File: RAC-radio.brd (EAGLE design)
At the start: 160 x 100 mm, 24 parts, among them J2 CORTEX_DEBUG_MINIMUM_SMD, J3 U.FL, U1 MAX32660GTP+, U2 RN4871-I_RM130, U3 RFM95W-868S2, Y1 32.768kHz

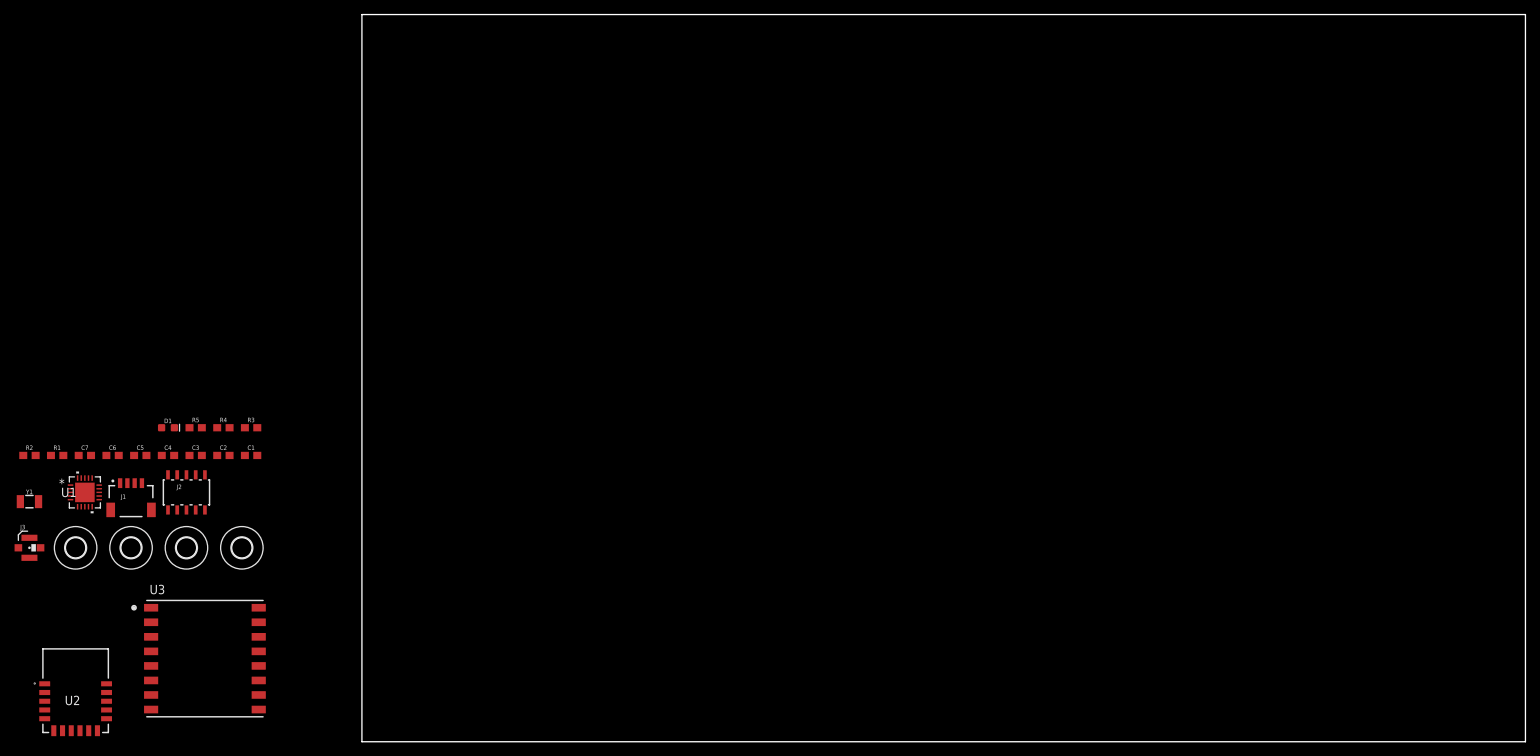
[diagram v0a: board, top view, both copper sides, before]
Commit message: Routed the non-power nets
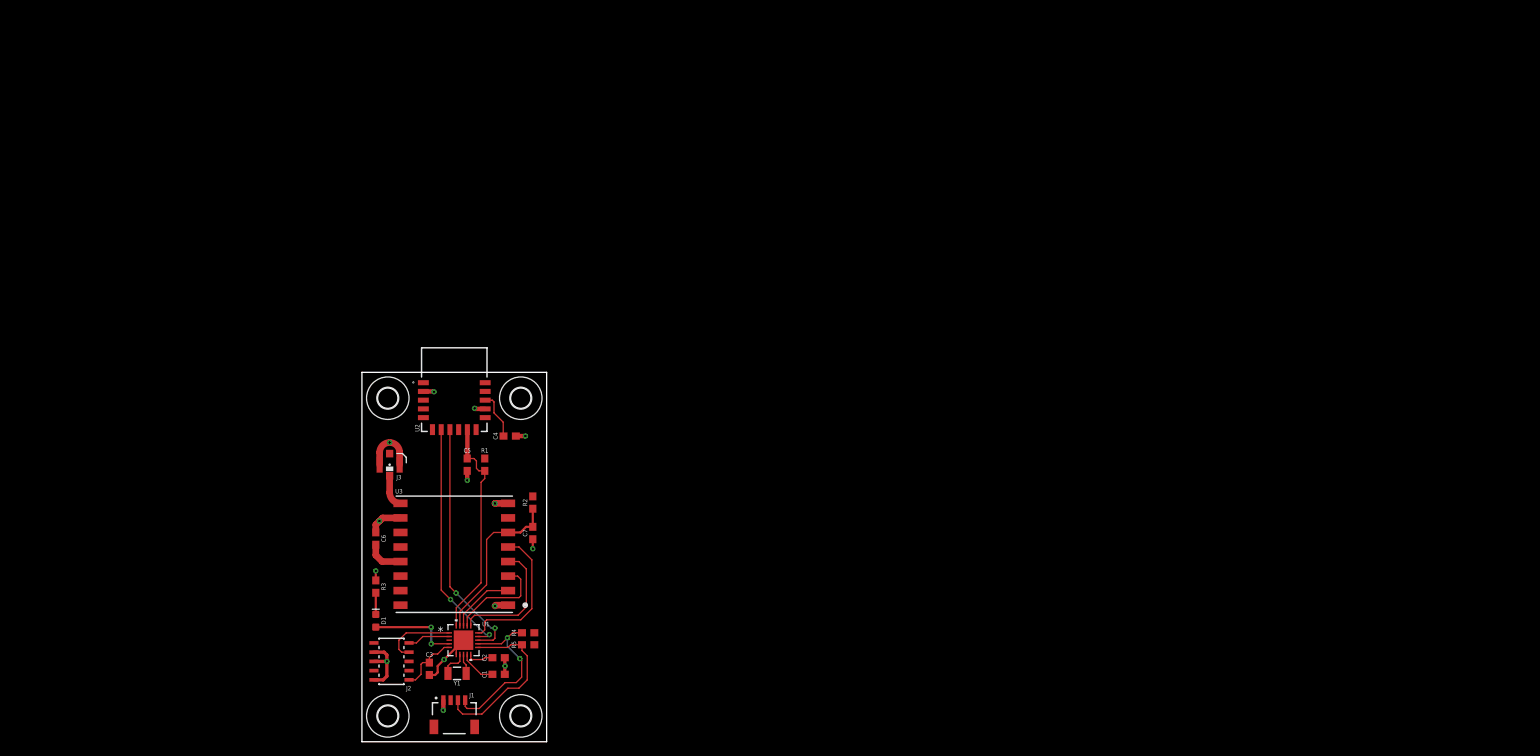
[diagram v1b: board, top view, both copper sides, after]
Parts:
- moved R2 69.5 mm to (23.5, 32.9), turned to 90 degrees
- moved U2 66.5 mm to (12.7, 42.7)
- moved H4 65.4 mm to (21.8, 3.56)
- moved Y1 63.4 mm to (13.1, 9.40), turned to 180 degrees
- moved C7 62.5 mm to (23.5, 28.7), turned to 270 degrees
- moved R1 58.8 mm to (16.9, 38.1), turned to 90 degrees
- moved U1 55.9 mm to (14.0, 14.0)
- moved R5 54.6 mm to (22.9, 13.3)
- moved J1 53.5 mm to (12.7, 5.71)
- moved J3 50.8 mm to (3.81, 38.1), turned to 270 degrees
- moved R4 50.5 mm to (22.9, 15.0)
- moved H2 50.4 mm to (21.8, 47.2)
- moved C4 47.1 mm to (20.3, 42.0)
- moved C2 47.0 mm to (18.8, 11.6)
- moved C1 45.4 mm to (18.8, 9.27)
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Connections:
- net N$2 renamed LED_CATH
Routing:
- net GND: track 0.00 -> 45.9 mm, vias 0 -> 14
- net UART1_RX: track 0.00 -> 34.0 mm, vias 0 -> 2
- net UART1_TX: track 0.00 -> 32.9 mm, vias 0 -> 2
- net !BT_RST: track 0.00 -> 30.6 mm
- net I2C0_SDA: track 0.00 -> 24.4 mm
- net I2C0_SCL: track 0.00 -> 23.5 mm, vias 0 -> 2
- net !LORA_RST: track 0.00 -> 23.0 mm
- net !SPI0_CS: track 0.00 -> 20.2 mm
- net SPI0_SCK: track 0.00 -> 17.4 mm
- net VCC: track 0.00 -> 16.8 mm
- net SPI0_MOSI: track 0.00 -> 14.0 mm
- net IO_LED: track 0.00 -> 12.4 mm, vias 0 -> 2
- net SWDCLK: track 0.00 -> 10.2 mm
- net SPI0_MISO: track 0.00 -> 9.07 mm
- net !MCU_RST: track 0.00 -> 8.59 mm
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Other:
- board size 160 x 100 mm -> 25.4 x 50.8 mm

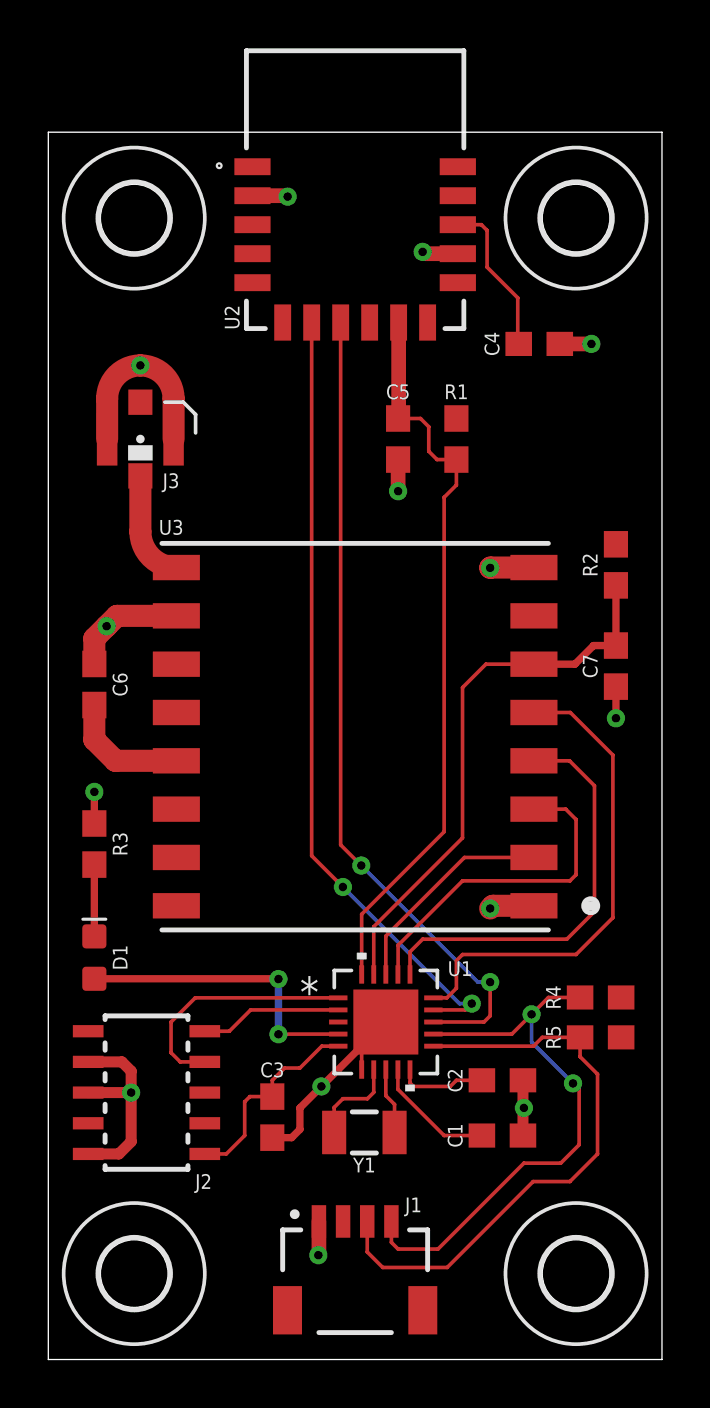
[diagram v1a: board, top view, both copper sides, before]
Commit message: Finished routing board, cleared DRC
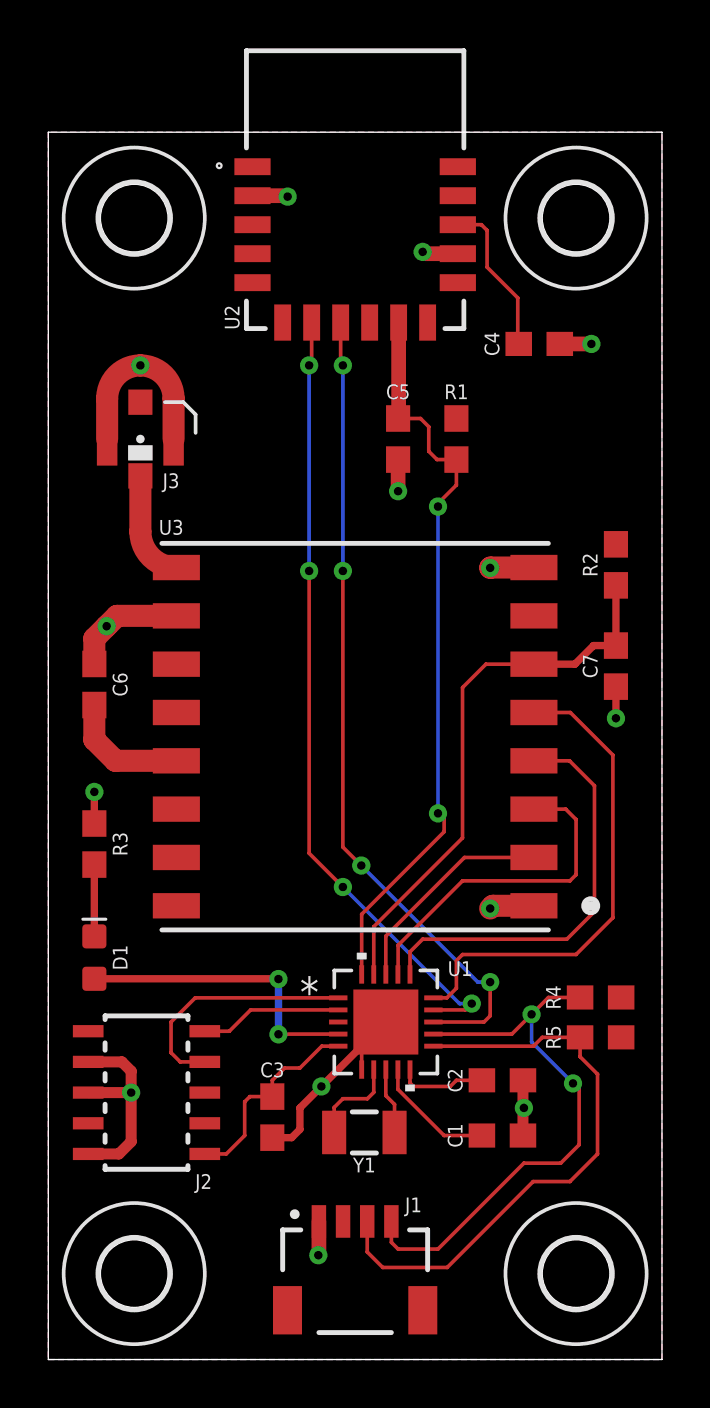
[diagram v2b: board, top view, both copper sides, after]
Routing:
- net !BT_RST: track 30.6 -> 30.8 mm, vias 0 -> 2
- net UART1_TX: track 32.9 -> 33.0 mm, vias 2 -> 4
- net UART1_RX: vias 2 -> 4
- added copper zone on layer 16, net GND
- added copper zone on layer 1, net VCC
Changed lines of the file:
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@@
 <wire x1="25.4" y1="50.8" x2="0" y2="50.8" width="0" layer="20"/>
 <wire x1="0" y1="50.8" x2="0" y2="0" width="0" layer="20"/>
+<polygon width="0.1524" layer="41">
+<vertex x="14.351" y="12.319"/>
+<vertex x="14.351" y="11.176"/>
+<vertex x="16.383" y="9.144"/>
+<vertex x="17.399" y="9.144"/>
+<vertex x="17.399" y="9.398"/>
+<vertex x="16.51" y="9.398"/>
+<vertex x="14.605" y="11.303"/>
+<vertex x="14.605" y="12.319"/>
+</polygon>
+<polygon width="0.1524" layer="41">
+<vertex x="16.256" y="47.371"/>
+<vertex x="16.256" y="46.609"/>
+<vertex x="17.653" y="46.609"/>
+<vertex x="17.653" y="46.863"/>
+<vertex x="17.907" y="46.863"/>
+<vertex x="18.034" y="46.736"/>
+<vertex x="18.034" y="45.212"/>
+<vertex x="19.304" y="43.942"/>
+<vertex x="19.304" y="43.815"/>
+<vertex x="19.304" y="42.545"/>
+<vertex x="19.558" y="42.545"/>
+<vertex x="19.558" y="43.942"/>
+<vertex x="18.288" y="45.212"/>
+<vertex x="18.288" y="45.593"/>
+<vertex x="18.288" y="46.736"/>
+<vertex x="17.907" y="47.117"/>
+<vertex x="17.653" y="47.117"/>
+<vertex x="17.653" y="47.371"/>
+</polygon>
+<polygon width="0.1524" layer="41">
+<vertex x="4.318" y="25.273"/>
+<vertex x="6.223" y="25.273"/>
+<vertex x="6.223" y="24.257"/>
+<vertex x="4.318" y="24.257"/>
+<vertex x="2.667" y="24.257"/>
+<vertex x="1.397" y="25.527"/>
+<vertex x="1.397" y="26.543"/>
+<vertex x="2.413" y="26.543"/>
+<vertex x="2.413" y="25.908"/>
+<vertex x="3.048" y="25.273"/>
+</polygon>
 </plain>
 <attributes>
@@
 <wire x1="11.2" y1="4.342" x2="11.176" y2="4.318" width="0.6096" layer="1"/>
 <via x="11.176" y="4.318" extent="1-16" drill="0.35"/>
-<wire x1="16.95" y1="45.772" x2="21.17" y2="42.037" width="0" layer="19" extent="1-1"/>
-<wire x1="9.906" y1="48.133" x2="15.494" y2="45.847" width="0" layer="19" extent="1-1"/>
-<wire x1="14.478" y1="37.25" x2="21.17" y2="42.037" width="0" layer="19" extent="1-1"/>
-<wire x1="18.303" y1="32.781" x2="14.478" y2="35.941" width="0" layer="19" extent="1-1"/>
-<wire x1="23.495" y1="27.852" x2="20.1" y2="32.781" width="0" layer="19" extent="1-1"/>
-<wire x1="3.81" y1="41.148" x2="8.45" y2="48.172" width="0" layer="19" extent="1-1"/>
-<wire x1="5.3" y1="30.781" x2="5.185" y2="38.1" width="0" layer="19" extent="1-1"/>
-<wire x1="1.905" y1="23.495" x2="1.905" y2="28.79" width="0" layer="19" extent="1-1"/>
-<wire x1="20.1" y1="18.781" x2="23.495" y2="26.543" width="0" layer="19" extent="1-1"/>
-<wire x1="13.97" y1="13.97" x2="18.288" y2="18.669" width="0" layer="19" extent="1-1"/>
-<wire x1="11.2" y1="5.715" x2="10.072" y2="9.183" width="0" layer="19" extent="1-1"/>
-<wire x1="3.429" y1="9.017" x2="9.271" y2="9.183" width="0" layer="19" extent="1-1"/>
-<wire x1="19.646" y1="11.557" x2="13.97" y2="13.97" width="0" layer="19" extent="1-1"/>
+<polygon width="0.1524" layer="16" isolate="0.0007625">
+<vertex x="0" y="0"/>
+<vertex x="25.4" y="0"/>
+<vertex x="25.4" y="50.8"/>
+<vertex x="0" y="50.8"/>
+</polygon>
 </signal>
 <signal name="32KIN">
@@
 <wire x1="19.431" y1="43.942" x2="18.161" y2="45.212" width="0.1524" layer="1"/>
 <wire x1="18.161" y1="45.212" x2="18.161" y2="46.736" width="0.1524" layer="1"/>
-<wire x1="16.891" y1="38.95" x2="19.47" y2="42.037" width="0" layer="19" extent="1-1"/>
-<wire x1="23.495" y1="33.743" x2="16.891" y2="38.95" width="0" layer="19" extent="1-1"/>
-<wire x1="5.3" y1="24.781" x2="16.891" y2="38.95" width="0" layer="19" extent="1-1"/>
-<wire x1="1.651" y1="13.589" x2="2.778" y2="24.781" width="0" layer="19" extent="1-1"/>
-<wire x1="14.47" y1="12.0015" x2="1.651" y2="13.589" width="0" layer="19" extent="1-1"/>
-<wire x1="12.2" y1="5.715" x2="16.383" y2="9.271" width="0" layer="19" extent="1-1"/>
-<wire x1="23.71" y1="13.335" x2="17.946" y2="9.271" width="0" layer="19" extent="1-1"/>
-<wire x1="23.71" y1="14.986" x2="23.71" y2="13.335" width="0" layer="19" extent="1-1"/>
+<polygon width="0.1524" layer="1" isolate="0.0007625">
+<vertex x="0" y="0"/>
+<vertex x="25.4" y="0"/>
+<vertex x="25.4" y="50.8"/>
+<vertex x="0" y="50.8"/>
+</polygon>
 </signal>
 <signal name="I2C0_SCL">
@@
 <contactref element="U1" pad="14"/>
 <contactref element="U2" pad="7"/>
-<wire x1="10.9" y1="42.922" x2="10.9" y2="20.85" width="0.1524" layer="1"/>
-<wire x1="10.9" y1="20.85" x2="12.192" y2="19.558" width="0.1524" layer="1"/>
 <via x="12.192" y="19.558" extent="1-16" drill="0.35"/>
 <wire x1="12.192" y1="19.558" x2="17.018" y2="14.732" width="0.1524" layer="16"/>
@@
 <wire x1="15.9385" y1="14.47" x2="17.264" y2="14.47" width="0.1524" layer="1"/>
 <wire x1="17.264" y1="14.47" x2="17.526" y2="14.732" width="0.1524" layer="1"/>
+<wire x1="10.9" y1="42.922" x2="10.9" y2="41.253" width="0.1524" layer="1"/>
+<wire x1="10.9" y1="41.253" x2="10.795" y2="41.148" width="0.1524" layer="1"/>
+<via x="10.795" y="41.148" extent="1-16" drill="0.35"/>
+<wire x1="12.192" y1="19.558" x2="10.795" y2="20.955" width="0.1524" layer="1"/>
+<via x="10.795" y="32.639" extent="1-16" drill="0.35"/>
+<wire x1="10.795" y1="20.955" x2="10.795" y2="32.639" width="0.1524" layer="1"/>
+<wire x1="10.795" y1="41.148" x2="10.795" y2="32.639" width="0.1524" layer="16"/>
 </signal>
 <signal name="UART1_RX">
 <contactref element="U1" pad="13"/>
 <contactref element="U2" pad="8"/>
-<wire x1="12.1" y1="42.922" x2="12.1" y2="21.301" width="0.1524" layer="1"/>
-<wire x1="12.1" y1="21.301" x2="12.954" y2="20.447" width="0.1524" layer="1"/>
 <via x="12.954" y="20.447" extent="1-16" drill="0.35"/>
 <wire x1="12.954" y1="20.447" x2="17.78" y2="15.621" width="0.1524" layer="16"/>
@@
 <wire x1="18.288" y1="15.621" x2="18.288" y2="14.224" width="0.1524" layer="1"/>
 <wire x1="18.288" y1="14.224" x2="18.034" y2="13.97" width="0.1524" layer="1"/>
+<wire x1="12.1" y1="42.922" x2="12.1" y2="41.24" width="0.1524" layer="1"/>
+<wire x1="12.1" y1="41.24" x2="12.192" y2="41.148" width="0.1524" layer="1"/>
+<via x="12.192" y="41.148" extent="1-16" drill="0.35"/>
+<wire x1="12.954" y1="20.447" x2="12.192" y2="21.209" width="0.1524" layer="1"/>
+<via x="12.192" y="32.639" extent="1-16" drill="0.35"/>
+<wire x1="12.192" y1="21.209" x2="12.192" y2="32.639" width="0.1524" layer="1"/>
+<wire x1="12.192" y1="41.148" x2="12.192" y2="32.639" width="0.1524" layer="16"/>
 </signal>
 <signal name="!BT_RST">
@@
 <wire x1="15.748" y1="38.608" x2="15.406" y2="38.95" width="0.1524" layer="1"/>
 <wire x1="12.97" y1="15.9385" x2="12.97" y2="18.431" width="0.1524" layer="1"/>
-<wire x1="16.383" y1="35.687" x2="16.891" y2="36.195" width="0.1524" layer="1"/>
-<wire x1="16.891" y1="36.195" x2="16.891" y2="37.25" width="0.1524" layer="1"/>
+<wire x1="16.891" y1="37.25" x2="16.891" y2="36.195" width="0.1524" layer="1"/>
 <wire x1="12.97" y1="18.431" x2="16.383" y2="21.844" width="0.1524" layer="1"/>
-<wire x1="16.383" y1="21.844" x2="16.383" y2="35.687" width="0.1524" layer="1"/>
+<wire x1="16.383" y1="21.844" x2="16.383" y2="22.352" width="0.1524" layer="1"/>
+<wire x1="16.383" y1="22.352" x2="16.129" y2="22.606" width="0.1524" layer="1"/>
+<via x="16.129" y="22.606" extent="1-16" drill="0.35"/>
+<wire x1="16.129" y1="35.433" x2="16.129" y2="35.306" width="0.1524" layer="1"/>
+<via x="16.129" y="35.306" extent="1-16" drill="0.35"/>
+<wire x1="16.129" y1="35.306" x2="16.129" y2="22.606" width="0.1524" layer="16"/>
+<wire x1="16.891" y1="36.195" x2="16.129" y2="35.433" width="0.1524" layer="1"/>
 </signal>
 <signal name="!LORA_RST">
